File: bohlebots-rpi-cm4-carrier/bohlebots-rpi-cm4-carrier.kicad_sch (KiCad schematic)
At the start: 7 parts, among them J1 SI-46001-F, K1 Kicker, T1 Taster_LED, T2 Taster_LED, U1 Compute_Module_4_Connectors

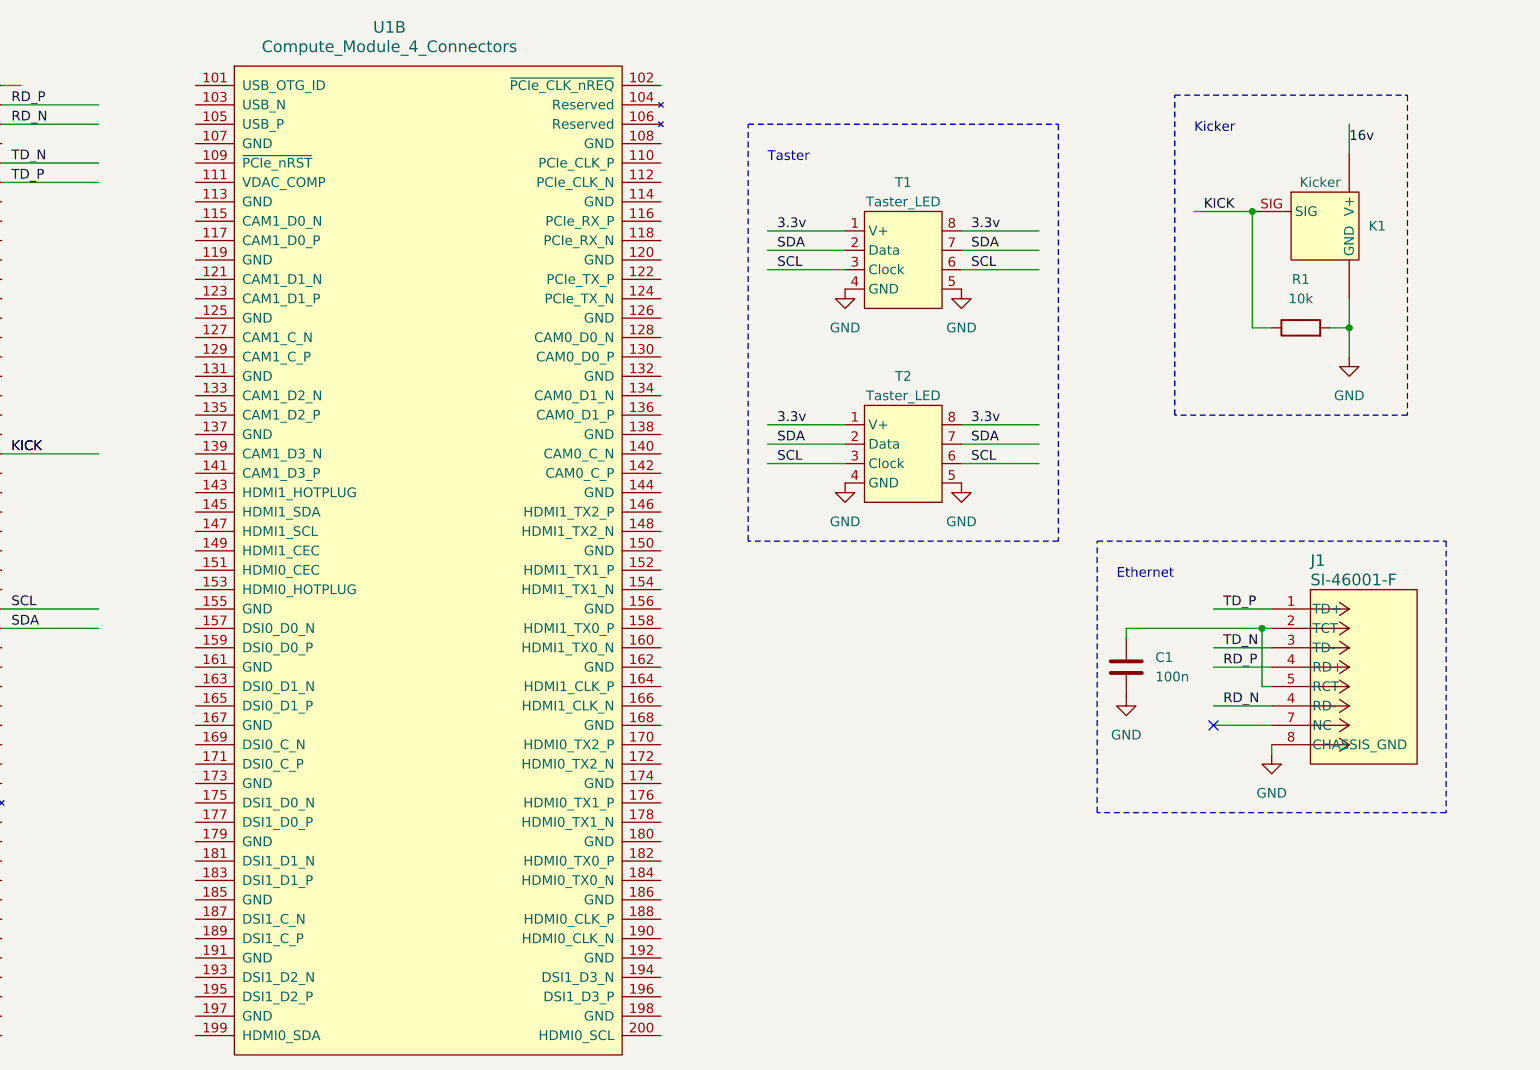
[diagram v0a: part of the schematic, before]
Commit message: Added USB and i2c connector for groundsensor.
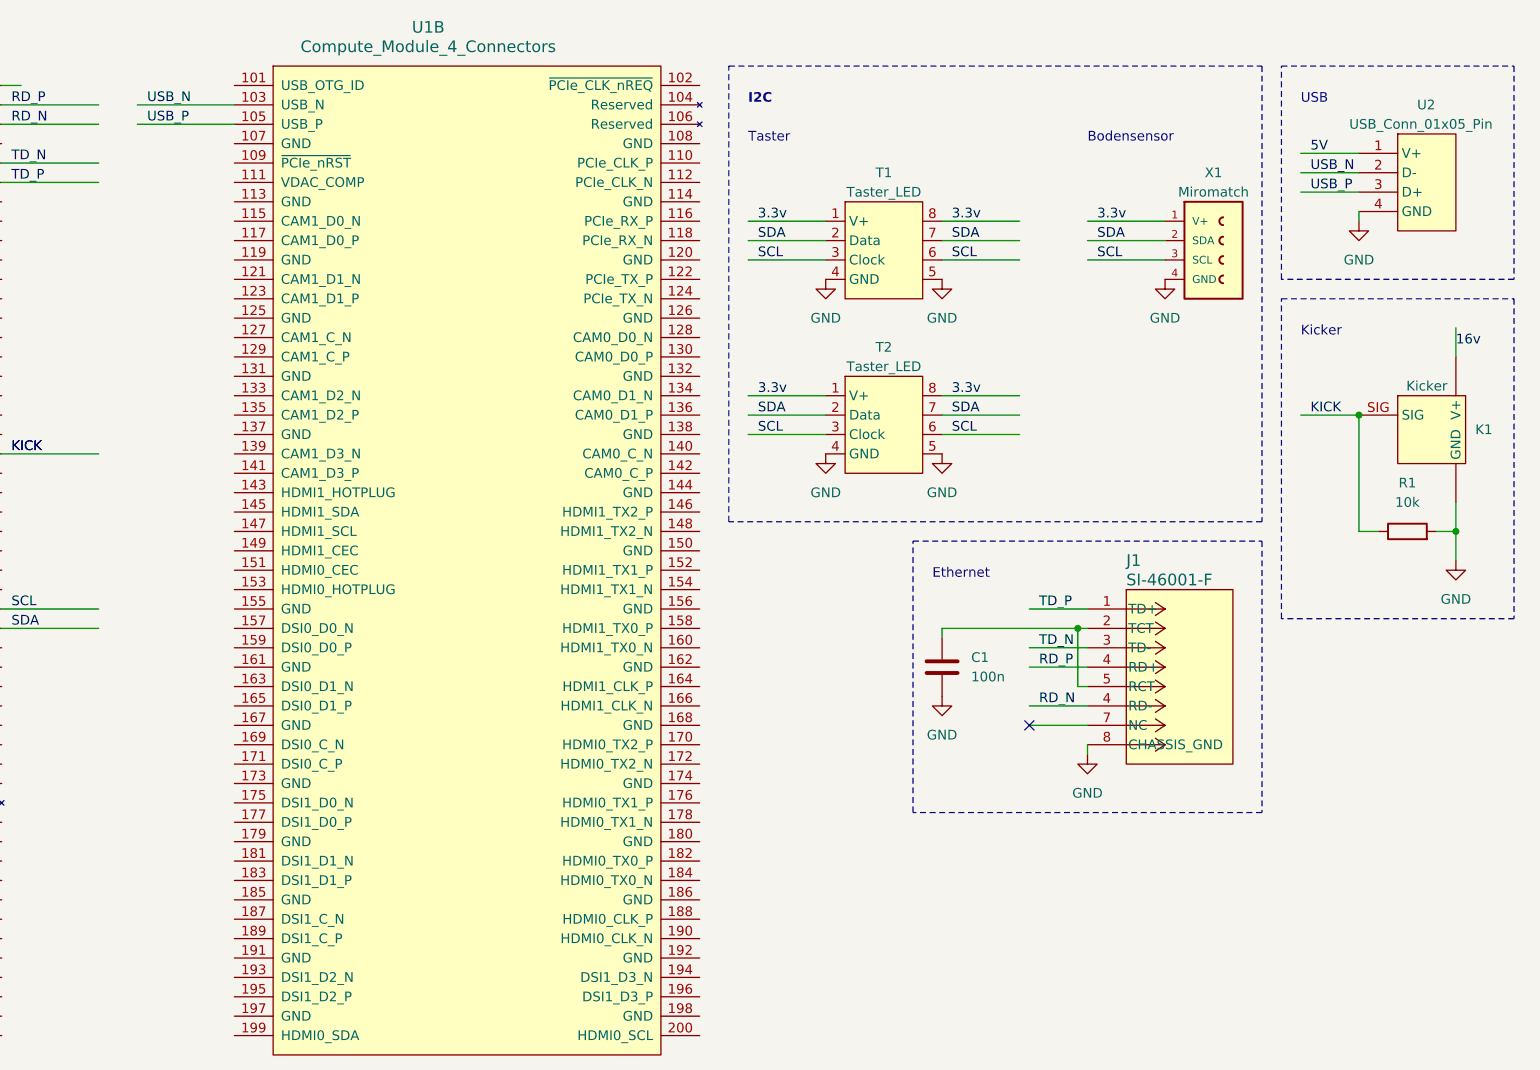
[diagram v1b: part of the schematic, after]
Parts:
- added U2: USB_Conn_01x05_Pin, Connector_PinHeader_2.54mm:PinHeader_1x05_P2.54mm_Vertical, symbol bohlebots-rpi-cm4-carrier-symbols:USB_Conn_01x05_Pin
- added X1: Miromatch, bohlebots:MICROMATCH-4, symbol bohlebots.lib:MICROMATCH-4
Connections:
- net 3.3v: now also X1.1 (V+)
- net GND: now also U2.4 (GND), X1.4 (GND)
- net SCL: now also X1.3 (SCL)
- net SDA: now also X1.2 (SDA)
- net USB_N: now reaches U1.103 (USB_N)
- net USB_N: now also U2.2 (D-)
- net USB_P: now reaches U1.105 (USB_P)
- net USB_P: now also U2.3 (D+)
- new net 5V: U2.1 (V+)
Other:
- note added: "Bodensensor"
- note added: "I2C"
- note added: "USB"
- moved on the sheet: C1, J1, K1, R1, T1, T2, U1B

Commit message: Added Motordrivers.
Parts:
- added ESCON1, ESCON2, ESCON3, ESCON4: 24_2, bohlebots:ESCOM_24_2, symbol bohlebots.lib:ESCOM_24/2
- added JP1, JP2, JP3, JP4: B8B-PH-K, bohlebots:B8B-PH-K, symbol main_backupboard-eagle-import:B8B-PH-K
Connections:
- net GND: now also ESCON1.P18 (GND), ESCON1.P5 (GND), ESCON2.P18 (GND), ESCON2.P5 (GND), ESCON3.P18 (GND), ESCON3.P5 (GND), ESCON4.P18 (GND), ESCON4.P5 (GND), JP1.5, JP2.5, JP3.5, JP4.5
- net PWM1: now reaches U1.24 (GPIO26)
- net PWM1: now also ESCON1.P17 (D1), ESCON2.P17 (D1), ESCON3.P17 (D1), ESCON4.P17 (D1)
- net PWM2: now reaches U1.26 (GPIO19)
- net PWM3: now reaches U1.28 (GPIO13)
- net PWM4: now reaches U1.30 (GPIO6)
- net ENA: now reaches U1.34 (GPIO5)
- net ENA: now also ESCON1.P16 (D2), ESCON2.P16 (D2), ESCON3.P16 (D2), ESCON4.P16 (D2)
- net DIR1: now reaches U1.44 (GPIO10)
- net DIR1: now also ESCON1.P15 (D3), ESCON2.P15 (D3), ESCON3.P15 (D3), ESCON4.P15 (D3)
- net DIR2: now reaches U1.46 (GPIO22)
- net DIR3: now reaches U1.48 (GPIO27)
- net DIR4: now reaches U1.50 (GPIO17)
- new net: ESCON3.P6 (+5V), JP3.1
- new net: ESCON3.P7 (H1), JP3.2
- new net: ESCON3.P9 (H3), JP3.3
- new net: ESCON3.P8 (H2), JP3.4
- new net: ESCON3.P3 (M3), JP3.6
- new net: ESCON3.P2 (M2), JP3.7
- new net: ESCON3.P1 (M1), JP3.8
- new net: ESCON1.P1 (M1), JP1.8
- new net: ESCON1.P2 (M2), JP1.7
- new net: ESCON1.P3 (M3), JP1.6
- new net: ESCON1.P6 (+5V), JP1.1
- new net: ESCON1.P7 (H1), JP1.2
- new net: ESCON1.P8 (H2), JP1.4
- new net: ESCON1.P9 (H3), JP1.3
- new net: ESCON4.P1 (M1), JP4.8
- new net: ESCON4.P2 (M2), JP4.7
- new net: ESCON4.P3 (M3), JP4.6
- new net: ESCON4.P6 (+5V), JP4.1
- new net: ESCON4.P7 (H1), JP4.2
- new net: ESCON4.P8 (H2), JP4.4
- new net: ESCON4.P9 (H3), JP4.3
- new net: ESCON2.P1 (M1), JP2.8
- new net: ESCON2.P2 (M2), JP2.7
- new net: ESCON2.P3 (M3), JP2.6
- new net: ESCON2.P6 (+5V), JP2.1
- new net: ESCON2.P7 (H1), JP2.2
- new net: ESCON2.P8 (H2), JP2.4
- new net: ESCON2.P9 (H3), JP2.3
- new net 16V: ESCON1.P4 (VCC), ESCON2.P4 (VCC), ESCON3.P4 (VCC), ESCON4.P4 (VCC)
- no-connect marks 1 -> 5
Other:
- note added: "Motortreiber"

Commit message: Save.
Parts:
- added C2: 100n, symbol Device:C
- added D36V28FX1: 5V, bohlebots:D36V28FX, symbol bohlebots.lib:D36V28FX
- added D36V28FX2: 3.3V, bohlebots:D36V28FX, symbol bohlebots.lib:D36V28FX
- added H1: Pinhead_1x04V, bohlebots:PinHeader_1x04_P2.54mm_Vertical, symbol bohlebots.lib:Pinhead_1x04V
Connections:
- net DIR1 is gone; now on net GND: ESCON1.P15 (D3), ESCON2.P15 (D3), ESCON3.P15 (D3), ESCON4.P15 (D3), U1.44 (GPIO10)
- net DIR2 is gone; now on net GND: U1.46 (GPIO22)
- net DIR3 is gone; now on net GND: U1.48 (GPIO27)
- net DIR4 is gone; now on net GND: U1.50 (GPIO17)
- net ENA is gone; now on net GND: ESCON1.P16 (D2), ESCON2.P16 (D2), ESCON3.P16 (D2), ESCON4.P16 (D2), U1.34 (GPIO5)
- net KICK is gone; now on net GND: K1.SIG, R1.1, U1.40 (GPIO9)
- net PWM1 is gone; now on net GND: ESCON1.P17 (D1), ESCON2.P17 (D1), ESCON3.P17 (D1), ESCON4.P17 (D1), U1.24 (GPIO26)
- net PWM2 is gone; now on net GND: U1.26 (GPIO19)
- net PWM3 is gone; now on net GND: U1.28 (GPIO13)
- net PWM4 is gone; now on net GND: U1.30 (GPIO6)
- net RD_N is gone; now on net GND: J1.4 (RD-), U1.6 (Ethernet_Pair1_N)
- net RD_P is gone; now on net GND: J1.4 (RD-), U1.4 (Ethernet_Pair1_P)
- net SCL is gone; now on net GND: T1.3 (Clock), T1.6, T2.3 (Clock), T2.6, U1.56 (GPIO3), X1.3 (SCL)
- net SDA is gone; now on net GND: T1.2 (Data), T1.7, T2.2 (Data), T2.7, U1.58 (GPIO2), X1.2 (SDA)
- net TD_N is gone; now on net GND: J1.3 (TD-), U1.10 (Ethernet_Pair0_N)
- net TD_P is gone; now on net GND: J1.1 (TD+), U1.12 (Ethernet_Pair0_P)
- net GND: now also U1.1 (GND), U1.107 (GND), U1.108 (GND), U1.113 (GND), U1.114 (GND), U1.119 (GND), U1.120 (GND), U1.125 (GND), U1.126 (GND), U1.13 (GND), U1.131 (GND), U1.132 (GND), U1.137 (GND), U1.138 (GND), U1.14 (GND), U1.144 (GND), U1.150 (GND), U1.155 (GND), U1.156 (GND), U1.161 (GND), U1.162 (GND), U1.167 (GND), U1.168 (GND), U1.173 (GND), U1.174 (GND), U1.179 (GND), U1.180 (GND), U1.185 (GND), U1.186 (GND), U1.191 (GND), U1.192 (GND), U1.197 (GND), U1.198 (GND), U1.2 (GND), U1.22 (GND), U1.23 (GND), U1.32 (GND), U1.33 (GND), U1.42 (GND), U1.43 (GND), U1.52 (GND), U1.53 (GND), U1.59 (GND), U1.60 (GND), U1.65 (GND), U1.66 (GND), U1.7 (GND), U1.71 (GND), U1.74 (GND), U1.8 (GND), U1.98 (GND), C2.2, H1.4 (GND)
- new net: C2.1, H1.1 (VCC)
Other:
- note added: "16V Input"
- moved on the sheet: C1, ESCON1, ESCON2, ESCON3, ESCON4, J1, JP1, JP2, JP3, JP4, K1, R1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

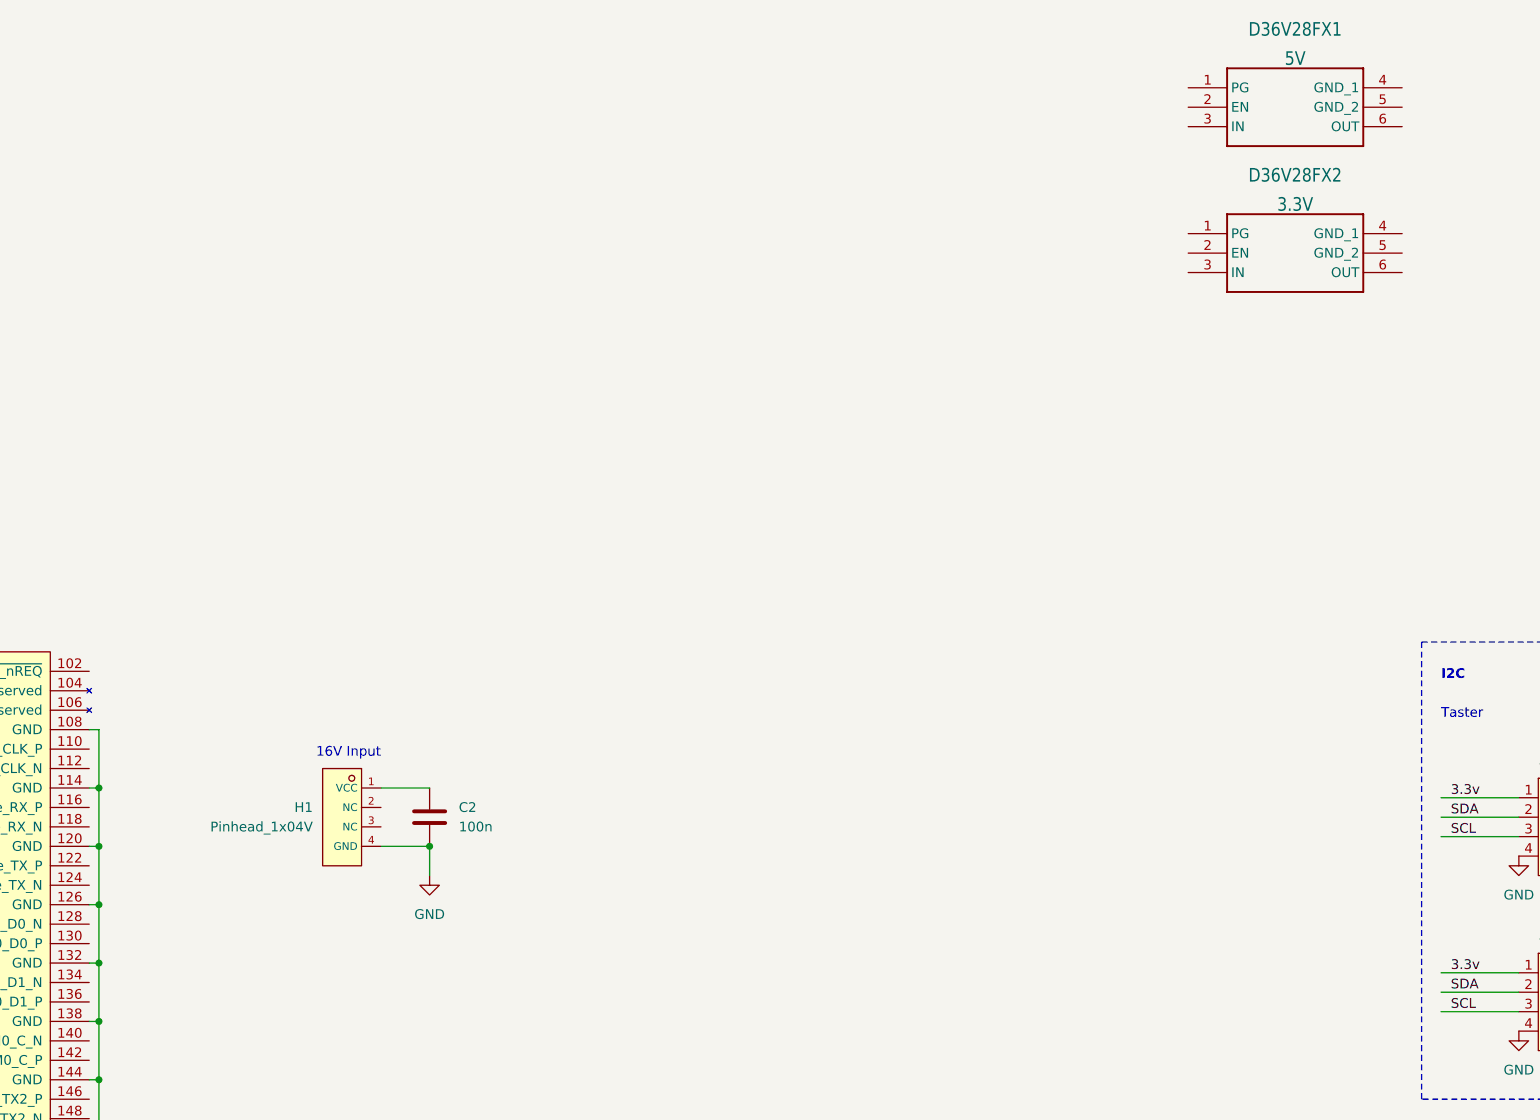
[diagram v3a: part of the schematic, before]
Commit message: Added step downs.
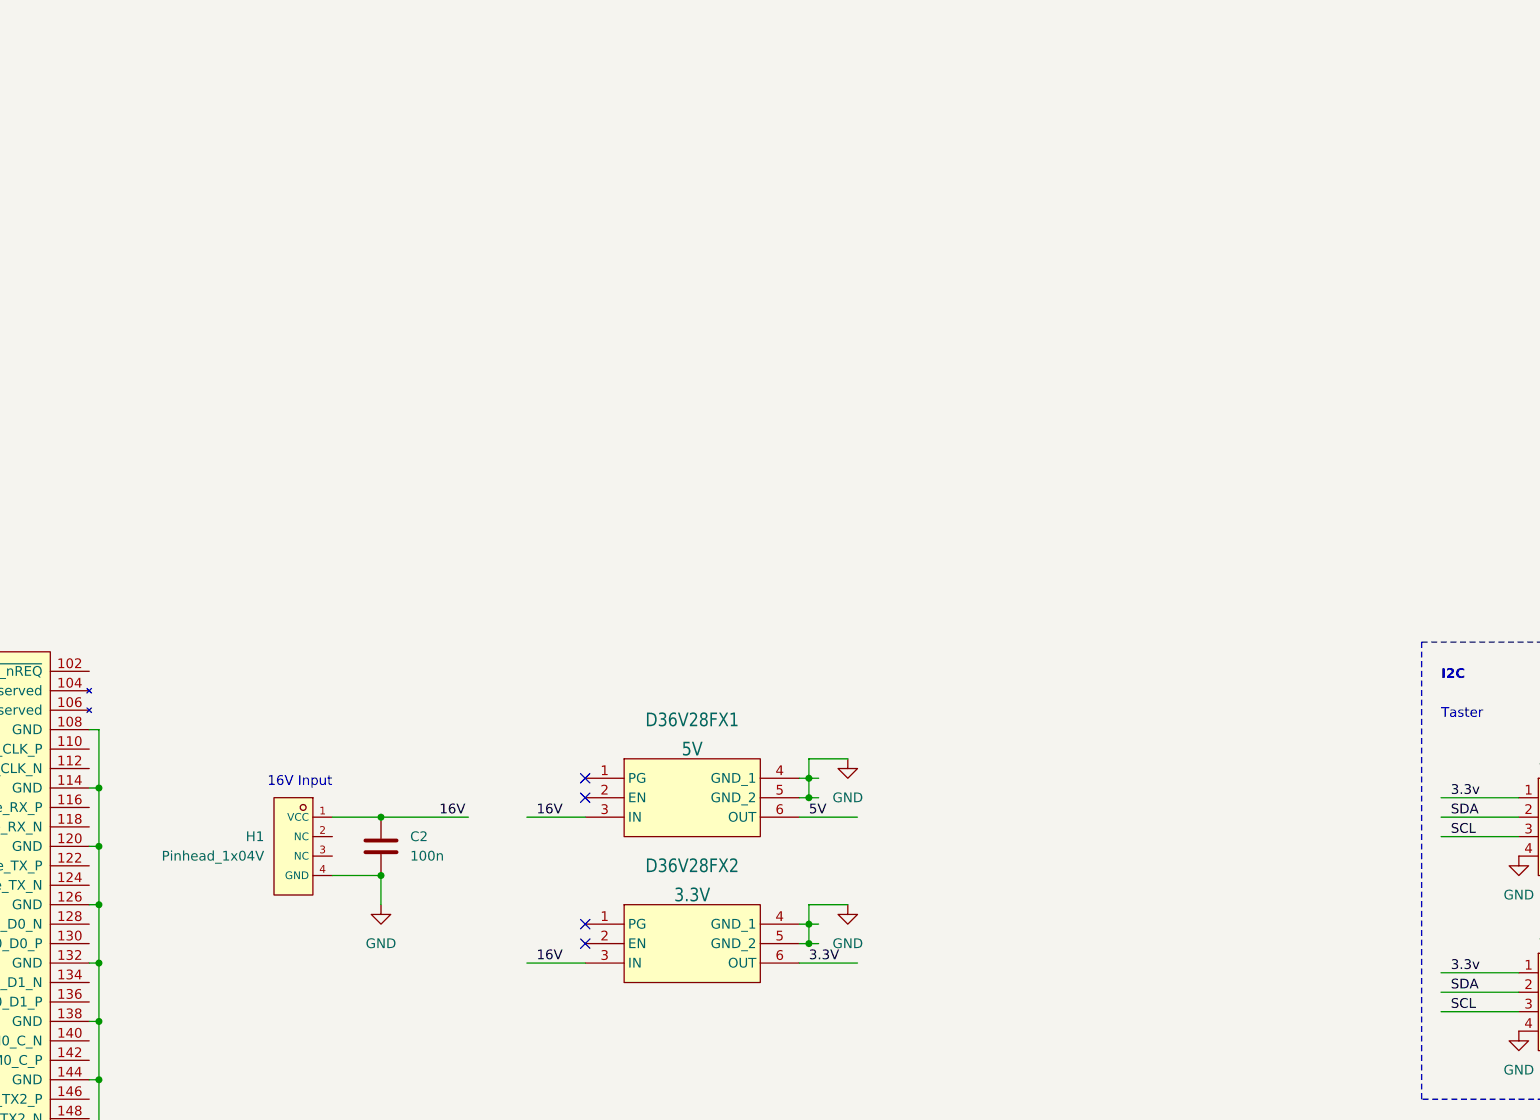
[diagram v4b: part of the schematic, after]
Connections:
- net 16V: now also C2.1, D36V28FX1.3 (IN), D36V28FX2.3 (IN), H1.1 (VCC)
- net 5V: now also D36V28FX1.6 (OUT)
- net GND: now also D36V28FX1.4 (GND_1), D36V28FX1.5 (GND_2), D36V28FX2.4 (GND_1), D36V28FX2.5 (GND_2)
- net 3.3V: now reaches D36V28FX2.6 (OUT)
- no-connect marks 5 -> 9
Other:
- moved on the sheet: C2, H1

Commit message: Added I2C pullup
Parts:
- added R2, R3: 10k, symbol Device:R
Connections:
- net 3.3V: now also R2.1, R3.1
- net GND: now also R2.2, R3.2
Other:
- note added: "I2C Pullup"
- note added: "PSU"
- note added: "Spannungsregler"
- note added: "place close to cm4"
- moved on the sheet: C1, C2, D36V28FX1, D36V28FX2, ESCON1, ESCON2, ESCON3, ESCON4, H1, J1, JP1, JP2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

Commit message: Some small changes, probably first finished schematic.
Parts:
- removed C2: 100n, symbol Device:C
- added J2: power_reference, Connector_PinHeader_2.54mm:PinHeader_1x02_P2.54mm_Vertical, symbol Connector_Generic:Conn_01x02
- added J3: REF_OUT_Conn_02x05, Connector_PinHeader_2.54mm:PinHeader_2x05_P2.54mm_Vertical, symbol Connector_Generic:Conn_02x05_Top_Bottom
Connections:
- net 16v is gone; now on net 16V: K1.V+1 (V+), K1.V+2 (V+), K1.V+3 (V+)
- net 16V: now also J2.1 (VCC)
- net 3.3V: now also J3.1 (3.3V)
- net 5V: now also U1.77 (+5V), U1.79 (+5V), U1.81 (+5V), U1.83 (+5V), U1.85 (+5V), U1.87 (+5V), J3.5 (5V)
- net GND: now also J2.2 (GND), J3.2 (SDA), J3.3 (SCL), J3.4 (GND)
- net RSV1: now reaches U1.25 (GPIO21)
- net RSV1: now also J3.6 (RSV1)
- net RSV2: now reaches U1.27 (GPIO20)
- net RSV2: now also J3.7 (RSV2)
- net RSV3: now reaches U1.29 (GPIO16)
- net RSV3: now also J3.8 (RSV3)
- net RSV4: now reaches U1.31 (GPIO12)
- net RSV4: now also J3.9 (RSV4)
- net at U1.84 (CM4_3.3V_Out): now also U1.86 (CM4_3.3V_Out)
- net at U1.88 (CM4_1.8V_Out): now also U1.90 (CM4_1.8V_Out)
- no-connect marks 9 -> 11
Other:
- note added: "Interfaces"
- note added: "Out pins for debug and extentions"
- note added: "Reserved GPIO pins"
- note added: "Reserved gpios get feed out for later usage"
- note added: "power_in"
- note added: "test voltage or connect voltmeter display"
- moved on the sheet: C1, D36V28FX1, D36V28FX2, ESCON1, ESCON2, ESCON3, ESCON4, H1, J1, JP1, JP2, JP3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
